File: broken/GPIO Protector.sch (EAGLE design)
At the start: 19 parts

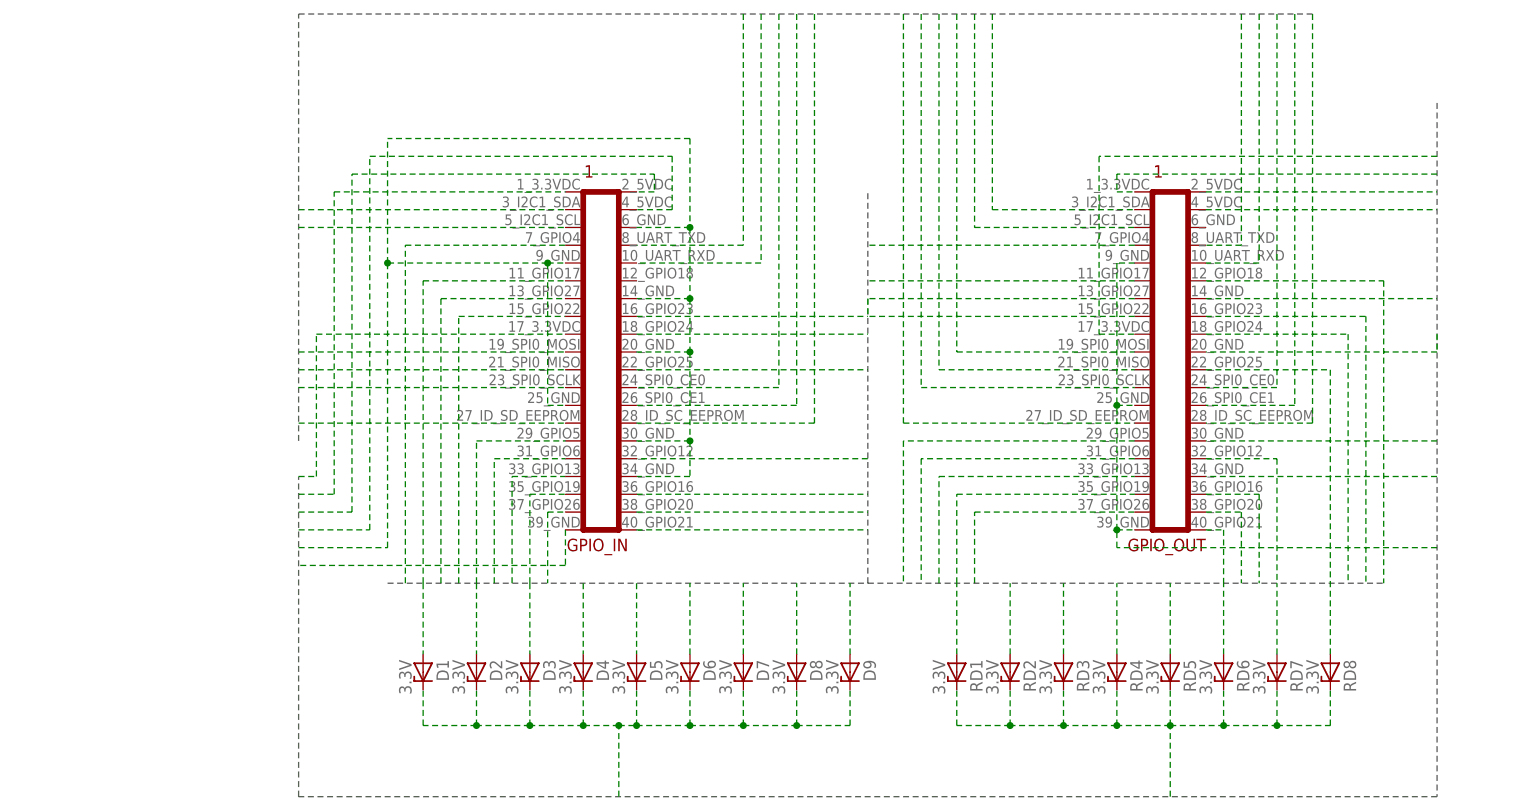
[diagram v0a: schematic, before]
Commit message: Moved some things to broken for now. May fix them later.
Added console to split protector in GPIO Split Protector with Console.

Added Arduino Detectors shield.
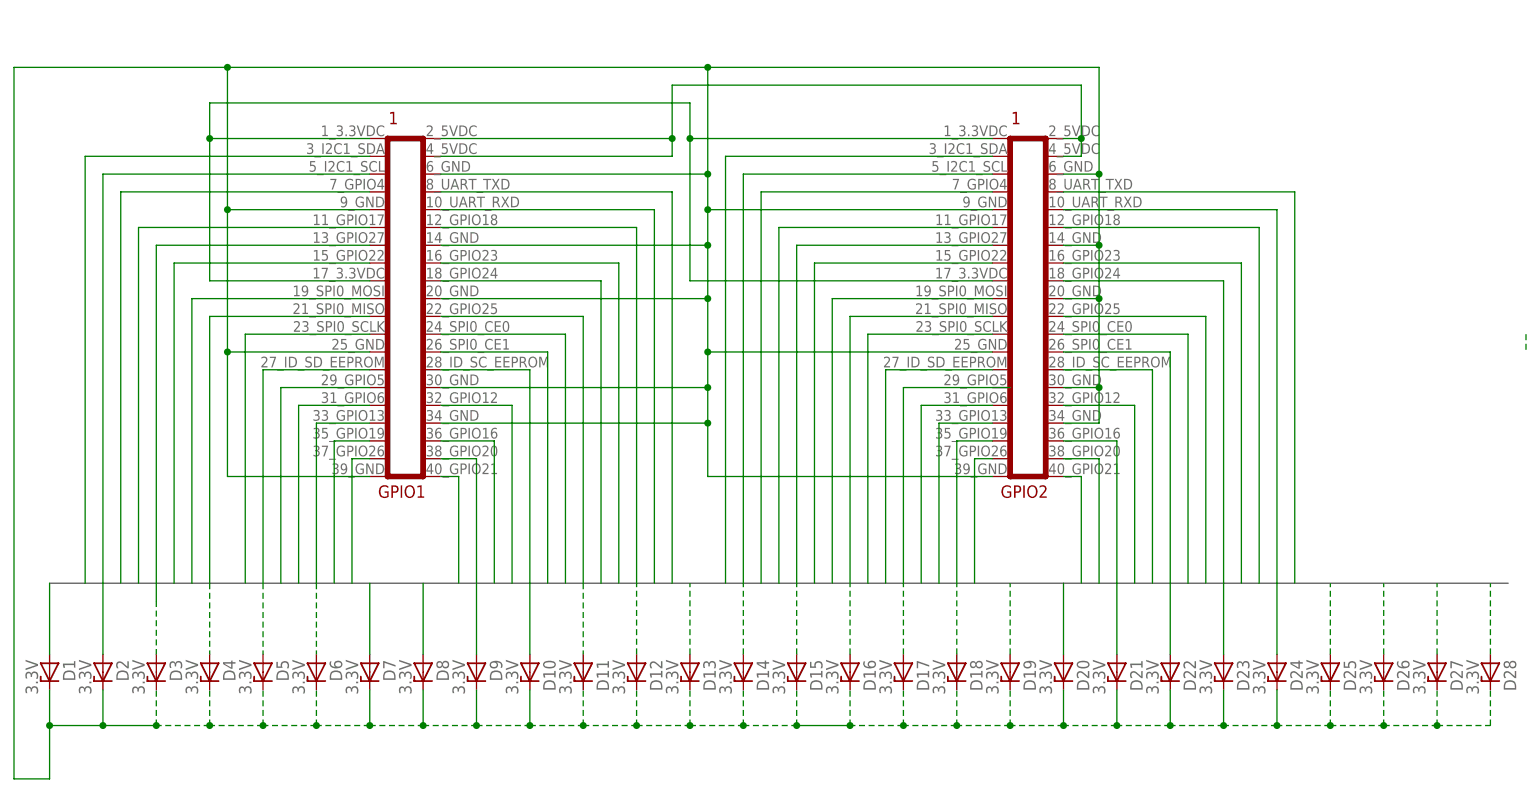
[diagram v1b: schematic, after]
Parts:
- removed GPIO_IN, GPIO_OUT: RPI_GPIOUPPER, connectors:RPI_GPIOUPPER
- added D10, D11, D12, D13, D14, D15, D16, D17, D26, D27, D28: 3.3V, diode:ZENER-DIODEDO41Z10
- added GPIO1, GPIO2: RPI_GPIOUPPER, connectors:RPI_GPIOUPPER
- renumbered RD1 to D18, RD2 to D19, RD3 to D20, RD4 to D21, RD5 to D22, RD6 to D23, RD7 to D24, RD8 to D25
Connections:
- removed net 3.3VDC1: GPIO_IN.1_3.3VDC, GPIO_OUT.1_3.3VDC
- removed net 3.3VDC2: GPIO_IN.17_3.3VDC, GPIO_OUT.17_3.3VDC
- removed net 5VDC1: GPIO_IN.2_5VDC, GPIO_OUT.2_5VDC
- removed net 5VDC2: GPIO_IN.4_5VDC, GPIO_OUT.4_5VDC
- removed net I2C1_SCL: GPIO_IN.5_I2C1_SCL, GPIO_OUT.5_I2C1_SCL
- removed net I2C1_SDA: GPIO_IN.3_I2C1_SDA, GPIO_OUT.3_I2C1_SDA
- removed net SPI0_CE0: GPIO_IN.24_SPI0_CE0, GPIO_OUT.24_SPI0_CE0
- removed net SPI0_CE1: GPIO_IN.26_SPI0_CE1, GPIO_OUT.26_SPI0_CE1
- removed net SPI0_MOSI: GPIO_IN.19_SPI0_MOSI, GPIO_OUT.19_SPI0_MOSI
- removed net SPI0_SCLK: GPIO_IN.23_SPI0_SCLK, GPIO_OUT.23_SPI0_SCLK
- removed net SPIO_MISO: GPIO_IN.21_SPI0_MISO, GPIO_OUT.21_SPI0_MISO
- new net 3.3VDC: GPIO1.17_3.3VDC, GPIO1.1_3.3VDC, GPIO2.17_3.3VDC, GPIO2.1_3.3VDC
- new net 5VDC: GPIO1.2_5VDC, GPIO1.4_5VDC, GPIO2.2_5VDC, GPIO2.4_5VDC
- new net I2C_SCL: D2.A, GPIO1.5_I2C1_SCL, GPIO2.5_I2C1_SCL
- new net I2C_SDA: D1.A, GPIO1.3_I2C1_SDA, GPIO2.3_I2C1_SDA
- new net SPI_CE0: D22.A, GPIO1.24_SPI0_CE0, GPIO2.24_SPI0_CE0
- new net SPI_CE1: D23.A, GPIO1.26_SPI0_CE1, GPIO2.26_SPI0_CE1
- new net SPI_MISO: D8.A, GPIO1.21_SPI0_MISO, GPIO2.21_SPI0_MISO
- new net SPI_MOSI: D7.A, GPIO1.19_SPI0_MOSI, GPIO2.19_SPI0_MOSI
- new net SPI_SCLK: D9.A, GPIO1.23_SPI0_SCLK, GPIO2.23_SPI0_SCLK
- net GND: now also D10.C, D11.C, D12.C, D13.C, D14.C, D15.C, D16.C, D17.C, D26.C, D27.C, D28.C, GPIO1.14_GND, GPIO1.20_GND, GPIO1.25_GND, GPIO1.30_GND, GPIO1.34_GND, GPIO1.39_GND, GPIO1.6_GND, GPIO1.9_GND, GPIO2.14_GND, GPIO2.20_GND, GPIO2.25_GND, GPIO2.30_GND, GPIO2.34_GND, GPIO2.39_GND, GPIO2.6_GND, GPIO2.9_GND; no longer GPIO_IN.14_GND, GPIO_IN.20_GND, GPIO_IN.25_GND, GPIO_IN.30_GND, GPIO_IN.34_GND, GPIO_IN.39_GND, GPIO_IN.6_GND, GPIO_IN.9_GND, GPIO_OUT.14_GND, GPIO_OUT.20_GND, GPIO_OUT.25_GND, GPIO_OUT.30_GND, GPIO_OUT.34_GND, GPIO_OUT.39_GND, GPIO_OUT.9_GND
- net GPIO12: now also D25.A, GPIO1.32_GPIO12, GPIO2.32_GPIO12; no longer D22.A, GPIO_IN.32_GPIO12, GPIO_OUT.32_GPIO12
- net GPIO13: now also D13.A, GPIO1.33_GPIO13, GPIO2.33_GPIO13; no longer D7.A, GPIO_IN.33_GPIO13, GPIO_OUT.33_GPIO13
- net GPIO16: now also D26.A, GPIO1.36_GPIO16, GPIO2.36_GPIO16; no longer D23.A, GPIO_IN.36_GPIO16, GPIO_OUT.36_GPIO16
- net GPIO17: now also D4.A, GPIO1.11_GPIO17, GPIO2.11_GPIO17; no longer D2.A, GPIO_IN.11_GPIO17, GPIO_OUT.11_GPIO17
- net GPIO18: now also D16.A, GPIO1.12_GPIO18, GPIO2.12_GPIO18; no longer D18.A, GPIO_OUT.12_GPIO18
- net GPIO19: now also D14.A, GPIO1.35_GPIO19, GPIO2.35_GPIO19; no longer D8.A, GPIO_IN.35_GPIO19, GPIO_OUT.35_GPIO19
- net GPIO20: now also D27.A, GPIO1.38_GPIO20, GPIO2.38_GPIO20; no longer D24.A, GPIO_IN.38_GPIO20, GPIO_OUT.38_GPIO20
- net GPIO21: now also D28.A, GPIO1.40_GPIO21, GPIO2.40_GPIO21; no longer D25.A, GPIO_IN.40_GPIO21, GPIO_OUT.40_GPIO21
- net GPIO22: now also D6.A, GPIO1.15_GPIO22, GPIO2.15_GPIO22; no longer D4.A, GPIO_IN.15_GPIO22, GPIO_OUT.15_GPIO22
- net GPIO23: now also D17.A, GPIO1.16_GPIO23, GPIO2.16_GPIO23; no longer D19.A, GPIO_IN.16_GPIO23, GPIO_OUT.16_GPIO23
- net GPIO24: now also D18.A, GPIO1.18_GPIO24, GPIO2.18_GPIO24; no longer D20.A, GPIO_IN.18_GPIO24, GPIO_OUT.18_GPIO24
- net GPIO25: now also D19.A, GPIO1.22_GPIO25, GPIO2.22_GPIO25; no longer D21.A, GPIO_IN.22_GPIO25, GPIO_OUT.22_GPIO25
- net GPIO26: now also D15.A, GPIO1.37_GPIO26, GPIO2.37_GPIO26; no longer D9.A, GPIO_IN.37_GPIO26, GPIO_OUT.37_GPIO26
- net GPIO27: now also D5.A, GPIO1.13_GPIO27, GPIO2.13_GPIO27; no longer D3.A, GPIO_IN.13_GPIO27, GPIO_OUT.13_GPIO27
- net GPIO4: now also D3.A, GPIO1.7_GPIO4, GPIO2.7_GPIO4; no longer D1.A, GPIO_IN.7_GPIO4, GPIO_OUT.7_GPIO4
- net GPIO5: now also D11.A, GPIO1.29_GPIO5; no longer D5.A, GPIO_IN.29_GPIO5, GPIO_OUT.29_GPIO5
- net GPIO6: now also D12.A, GPIO1.31_GPIO6, GPIO2.31_GPIO6; no longer D6.A, GPIO_IN.31_GPIO6, GPIO_OUT.31_GPIO6
- net ID_SC: now also D24.A, GPIO1.28_ID_SC_EEPROM, GPIO2.28_ID_SC_EEPROM; no longer GPIO_IN.28_ID_SC_EEPROM, GPIO_OUT.28_ID_SC_EEPROM
- net ID_SD: now also D10.A, GPIO1.27_ID_SC_EEPROM, GPIO2.27_ID_SC_EEPROM; no longer GPIO_IN.27_ID_SC_EEPROM, GPIO_OUT.27_ID_SC_EEPROM
- net UART_RXD: now also D21.A, GPIO1.10_UART0_RXD, GPIO2.10_UART0_RXD; no longer GPIO_IN.10_UART0_RXD, GPIO_OUT.10_UART0_RXD
- net UART_TXD: now also D20.A, GPIO1.8_UART0_TXD, GPIO2.8_UART0_TXD; no longer GPIO_IN.8_UART0_TXD, GPIO_OUT.8_UART0_TXD
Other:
- moved on the sheet: D1, D2, D3, D4, D5, D6, D7, D8, D9
